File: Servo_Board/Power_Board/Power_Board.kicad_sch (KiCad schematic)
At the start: 59 parts

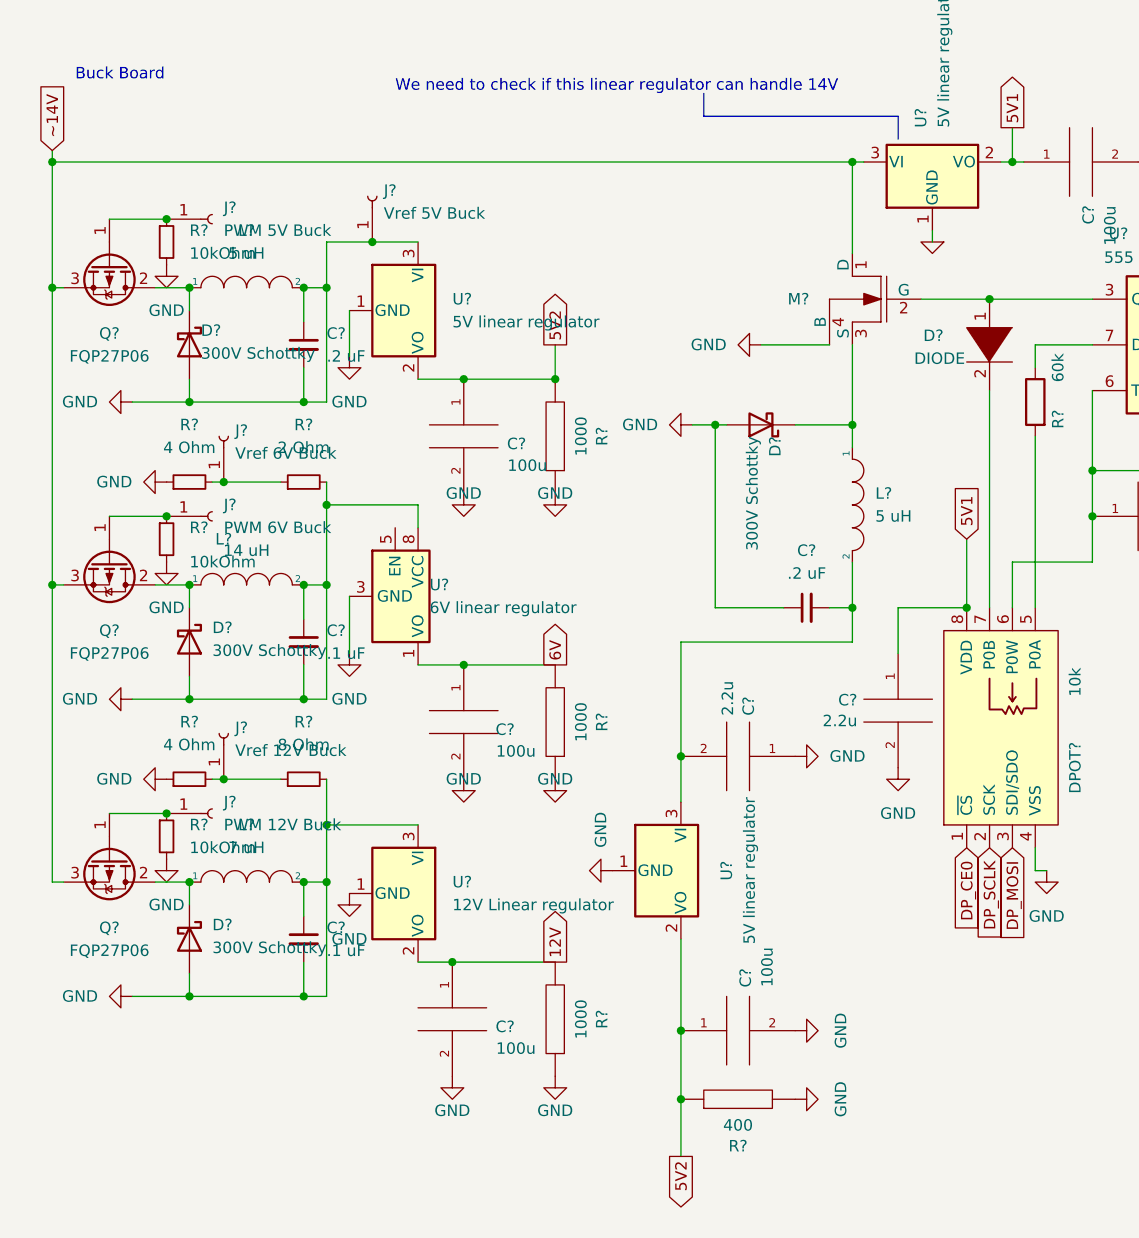
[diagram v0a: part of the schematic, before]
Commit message: Simplified our circuit, we'll only use 2 bucks
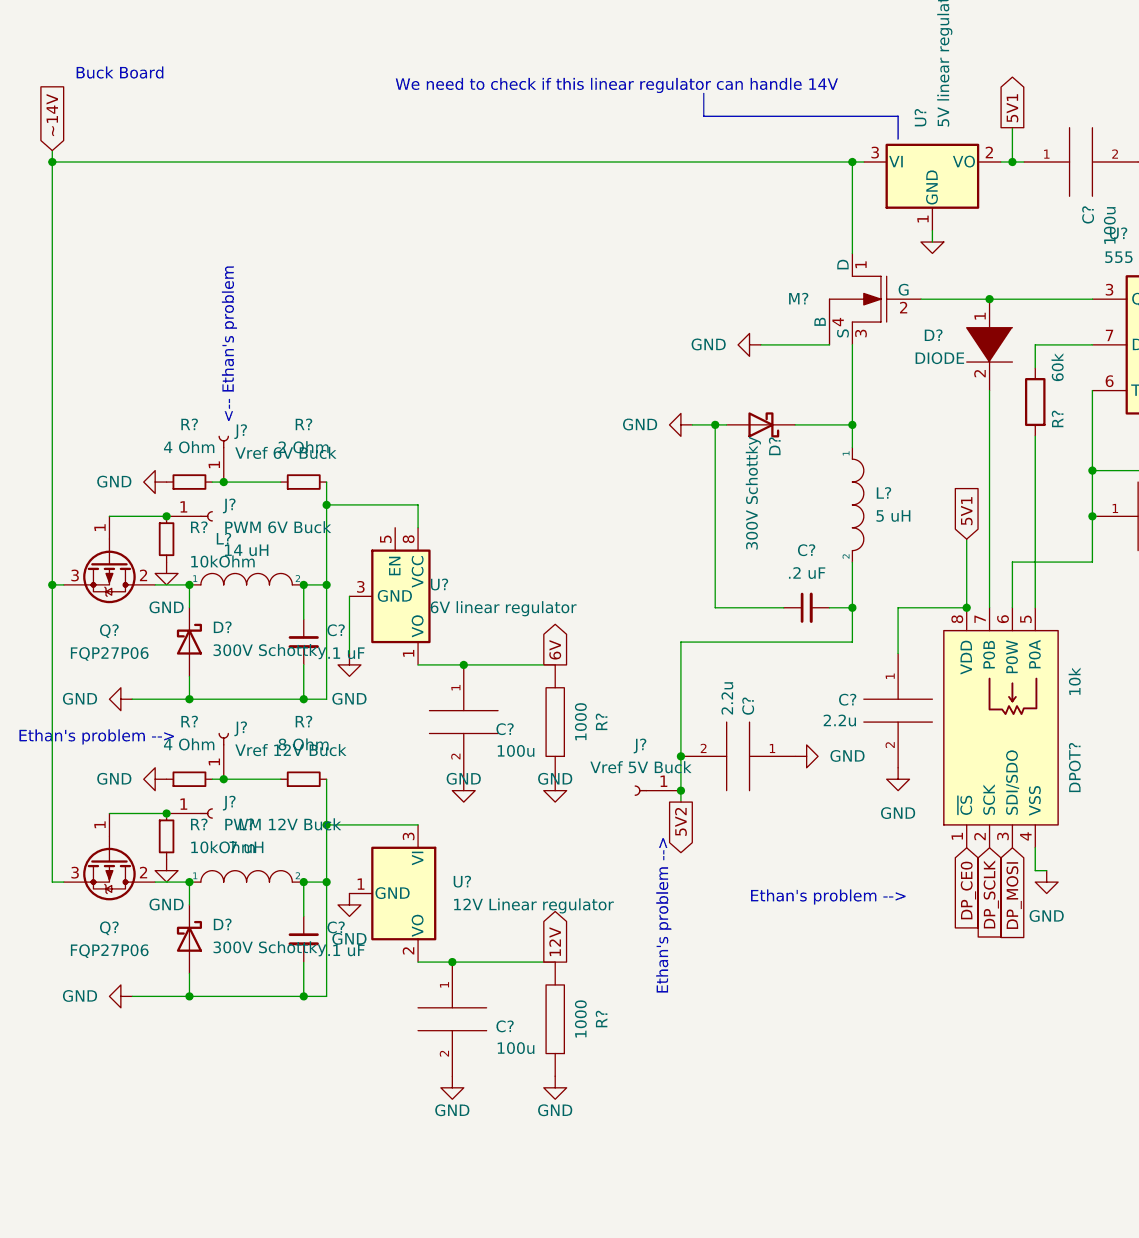
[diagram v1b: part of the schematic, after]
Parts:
- removed C? (x2): 100u, symbol pspice:CAP
- removed C?: .2 uF, symbol Device:C_Small
- removed D?: 300V Schottky, symbol Device:D_Schottky
- removed J?: Vref 5V Buck, symbol Connector:Conn_01x01_Female
- removed J?: PWM 5V Buck, symbol Connector:Conn_01x01_Female
- removed L?: 5 uH, symbol pspice:INDUCTOR
- removed Q?: FQP27P06, Package_TO_SOT_THT:TO-220-3_Vertical, symbol Transistor_FET:FQP27P06
- removed R?: 1000, symbol pspice:R
- removed R?: 400, symbol pspice:R
- removed R?: 10kOhm, symbol Device:R_Small
- removed U? (x2): 5V linear regulator, Package_TO_SOT_SMD:SOT-223-3_TabPin2, symbol Regulator_Linear:AMS1117-5.0
- added J?: Vref 5V Buck, symbol Connector:Conn_01x01_Female
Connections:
- net 5V2: now also C?.2, C?.2, L?.2, J?.1 (Pin_1)
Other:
- note added: "<-- Ethan's problem"
- note added: "Ethan's problem -->"

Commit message: Assignment ready update
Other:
- note added: "Please put your labeled component in this box"
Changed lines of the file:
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@@
+    (stroke (width 0) (type default) (color 0 0 0 0))
+  )
+  (polyline (pts (xy 11.43 139.7) (xy 120.65 139.7))
     (stroke (width 0) (type default) (color 0 0 0 0))
   )
@@
   )
   (wire (pts (xy 83.82 77.47) (xy 83.82 90.17))
+    (stroke (width 0) (type default) (color 0 0 0 0))
+  )
+  (polyline (pts (xy 120.65 139.7) (xy 120.65 198.12))
     (stroke (width 0) (type default) (color 0 0 0 0))
   )
@@
     (effects (font (size 1.27 1.27)) (justify left bottom))
   )
+  (text "Please put your labeled component in this box" (at 11.43 144.78 0)
+    (effects (font (size 3 3)) (justify left bottom))
+  )
   (text "Ethan's problem -->" (at 91.44 106.68 0)
